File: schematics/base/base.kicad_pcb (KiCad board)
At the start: 2 copper layers, 96.5 x 96.5 mm, 72 parts, among them J1 Bionic_ZIF_Socket_48pin, P10 P10, P11 P11, P12 P12, P13 P13, P14 P14, P15 P15, P16 P16, P17 P17, P20 P20, P21 P21, P22 P23, P23 P24, P24 P25, P25 P26, P26 P27, P27 P28, P30 P30, P31 P31, P32 P32, P33 P33, P34 P34, P35 P35, P36 P36, P37 P37, P40 P40, P41 P41, P42 P42, P43 P43, P44 P44, P45 P45, P46 P46, P47 P47, P50 P50, P51 P51, P52 P52, P53 P53, P54 P54, P55 P55, P56 P56, P57 P57, SW2 USR_SW, U1 TXS0108EPW, U2 TXS0108EPW, U3 TXS0108EPW, U4 TXS0108EPW, U5 TXS0108EPW, U6 SN74ACT1071DR, U7 SN74ACT1071DR

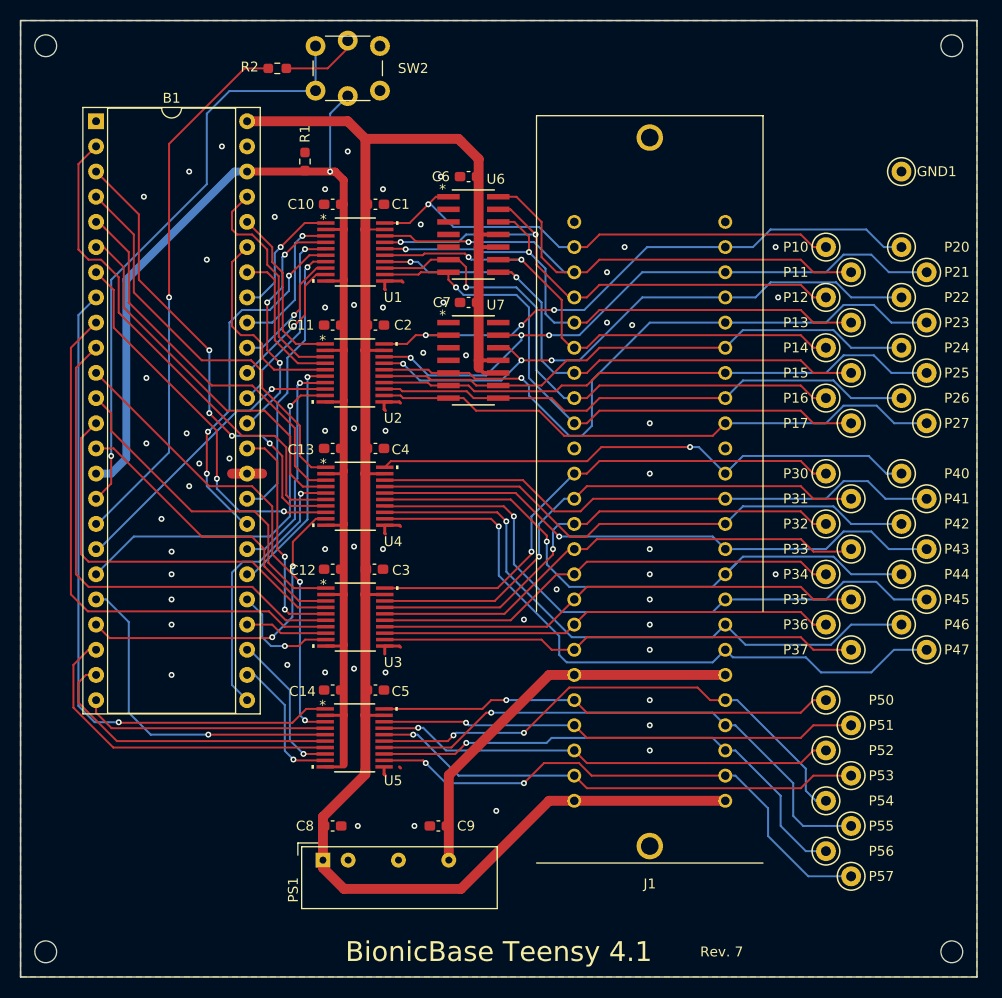
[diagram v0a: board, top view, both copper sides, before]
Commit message: [Base] Add USB-C Power connector
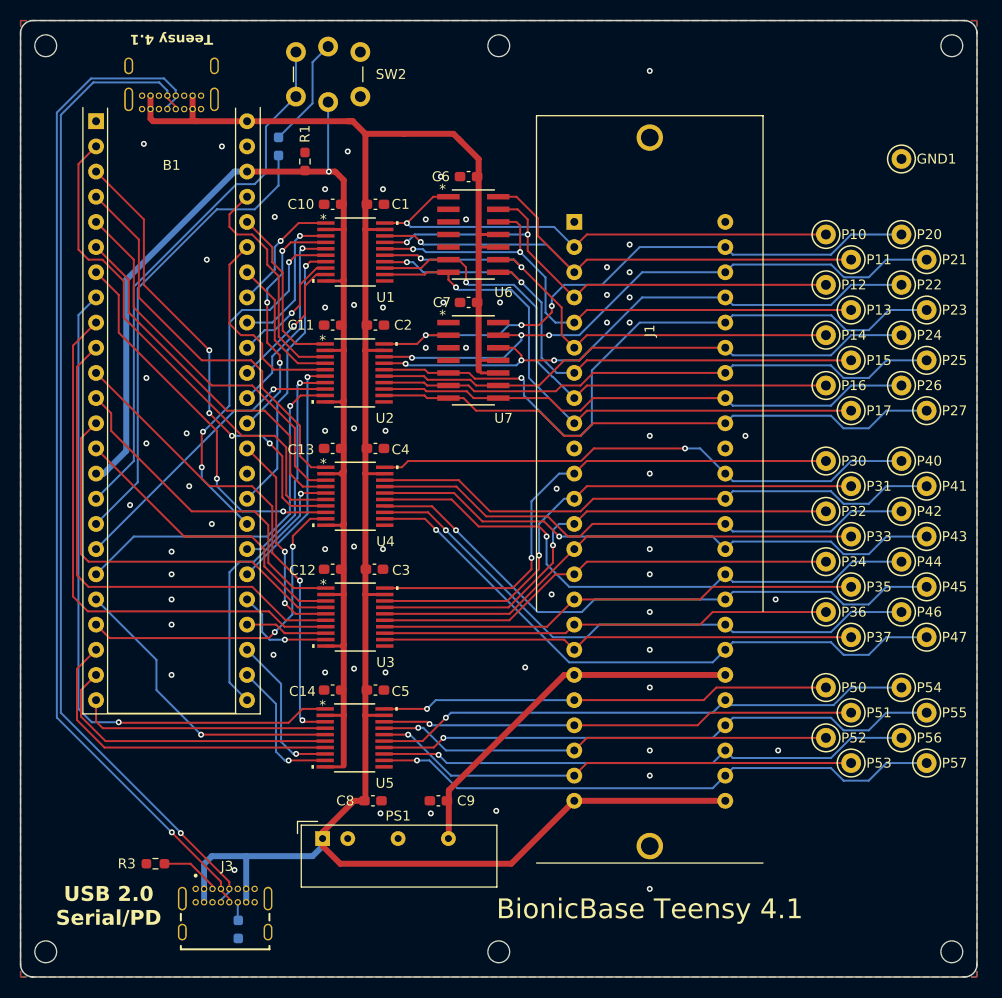
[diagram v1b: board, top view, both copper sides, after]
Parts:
- added J2: USB_C_USB2.0_16P, 0-LocalLibrary:GCT_USB4085-GF-A_REVB, B.Cu at (88.3, 46.6)
- added J3: USB_C_USB2.0_16P, 0-LocalLibrary:GCT_USB4085-GF-A_REVB, F.Cu at (93.7, 134.1)
- added MH2: MountingHole_2.2mm_M2, MountingHole:MountingHole_2.2mm_M2, F.Cu at (121.3, 136.0)
- added MH2: MountingHole_2.2mm_M2, MountingHole:MountingHole_2.2mm_M2, F.Cu at (121.3, 44.6)
- added R3: 5.1k, Resistor_SMD:R_0603_1608Metric_Pad0.98x0.95mm_HandSolder, F.Cu at (86.7, 127.2)
- added R4: 5.1k, Resistor_SMD:R_0603_1608Metric_Pad0.98x0.95mm_HandSolder, B.Cu at (95.0, 133.8)
- B1: footprint 0-LocalLibrary:DIP-48_W15.24mm_Socket -> 0-LocalLibrary:Teensy 4.1
- GND1: value GND -> TP; footprint TestPoint:TestPoint_Keystone_5000-5004_Miniature -> 0-LocalLibrary:TestPoint_Keystone_5001-black
- P10: value P10 -> TP; footprint TestPoint:TestPoint_Keystone_5000-5004_Miniature -> 0-LocalLibrary:TestPoint_Keystone_5001-black
- P11: value P11 -> TP; footprint TestPoint:TestPoint_Keystone_5000-5004_Miniature -> 0-LocalLibrary:TestPoint_Keystone_5115-brown
- P12: value P12 -> TP; footprint TestPoint:TestPoint_Keystone_5000-5004_Miniature -> 0-LocalLibrary:TestPoint_Keystone_5000-red
- P13: value P13 -> TP; footprint TestPoint:TestPoint_Keystone_5000-5004_Miniature -> 0-LocalLibrary:TestPoint_Keystone_5004-yellow
- P14: value P14 -> TP; footprint TestPoint:TestPoint_Keystone_5000-5004_Miniature -> 0-LocalLibrary:TestPoint_Keystone_5003-orange
- P15: value P15 -> TP; footprint TestPoint:TestPoint_Keystone_5000-5004_Miniature -> 0-LocalLibrary:TestPoint_Keystone_5116-green
- P16: value P16 -> TP; footprint TestPoint:TestPoint_Keystone_5000-5004_Miniature -> 0-LocalLibrary:TestPoint_Keystone_5117-blue
- P17: value P17 -> TP; footprint TestPoint:TestPoint_Keystone_5000-5004_Miniature -> 0-LocalLibrary:TestPoint_Keystone_5119-purple
- P20: value P20 -> TP; footprint TestPoint:TestPoint_Keystone_5000-5004_Miniature -> 0-LocalLibrary:TestPoint_Keystone_5001-black
- P21: value P21 -> TP; footprint TestPoint:TestPoint_Keystone_5000-5004_Miniature -> 0-LocalLibrary:TestPoint_Keystone_5115-brown
- P22: value P23 -> TP; footprint TestPoint:TestPoint_Keystone_5000-5004_Miniature -> 0-LocalLibrary:TestPoint_Keystone_5000-red
- P23: value P24 -> TP; footprint TestPoint:TestPoint_Keystone_5000-5004_Miniature -> 0-LocalLibrary:TestPoint_Keystone_5004-yellow
- P24: value P25 -> TP; footprint TestPoint:TestPoint_Keystone_5000-5004_Miniature -> 0-LocalLibrary:TestPoint_Keystone_5003-orange
- P25: value P26 -> TP; footprint TestPoint:TestPoint_Keystone_5000-5004_Miniature -> 0-LocalLibrary:TestPoint_Keystone_5116-green
- P26: value P27 -> TP; footprint TestPoint:TestPoint_Keystone_5000-5004_Miniature -> 0-LocalLibrary:TestPoint_Keystone_5117-blue
- P27: value P28 -> TP; footprint TestPoint:TestPoint_Keystone_5000-5004_Miniature -> 0-LocalLibrary:TestPoint_Keystone_5119-purple
- P30: value P30 -> TP; footprint TestPoint:TestPoint_Keystone_5000-5004_Miniature -> 0-LocalLibrary:TestPoint_Keystone_5001-black
- P31: value P31 -> TP; footprint TestPoint:TestPoint_Keystone_5000-5004_Miniature -> 0-LocalLibrary:TestPoint_Keystone_5115-brown
- P32: value P32 -> TP; footprint TestPoint:TestPoint_Keystone_5000-5004_Miniature -> 0-LocalLibrary:TestPoint_Keystone_5000-red
- P33: value P33 -> TP; footprint TestPoint:TestPoint_Keystone_5000-5004_Miniature -> 0-LocalLibrary:TestPoint_Keystone_5004-yellow
- P34: value P34 -> TP; footprint TestPoint:TestPoint_Keystone_5000-5004_Miniature -> 0-LocalLibrary:TestPoint_Keystone_5003-orange
- P35: value P35 -> TP; footprint TestPoint:TestPoint_Keystone_5000-5004_Miniature -> 0-LocalLibrary:TestPoint_Keystone_5116-green
- P36: value P36 -> TP; footprint TestPoint:TestPoint_Keystone_5000-5004_Miniature -> 0-LocalLibrary:TestPoint_Keystone_5117-blue
- P37: value P37 -> TP; footprint TestPoint:TestPoint_Keystone_5000-5004_Miniature -> 0-LocalLibrary:TestPoint_Keystone_5119-purple
- P40: value P40 -> TP; footprint TestPoint:TestPoint_Keystone_5000-5004_Miniature -> 0-LocalLibrary:TestPoint_Keystone_5001-black
- P41: value P41 -> TP; footprint TestPoint:TestPoint_Keystone_5000-5004_Miniature -> 0-LocalLibrary:TestPoint_Keystone_5115-brown
- P42: value P42 -> TP; footprint TestPoint:TestPoint_Keystone_5000-5004_Miniature -> 0-LocalLibrary:TestPoint_Keystone_5000-red
- P43: value P43 -> TP; footprint TestPoint:TestPoint_Keystone_5000-5004_Miniature -> 0-LocalLibrary:TestPoint_Keystone_5004-yellow
- P44: value P44 -> TP; footprint TestPoint:TestPoint_Keystone_5000-5004_Miniature -> 0-LocalLibrary:TestPoint_Keystone_5003-orange
- P45: value P45 -> TP; footprint TestPoint:TestPoint_Keystone_5000-5004_Miniature -> 0-LocalLibrary:TestPoint_Keystone_5116-green
- P46: value P46 -> TP; footprint TestPoint:TestPoint_Keystone_5000-5004_Miniature -> 0-LocalLibrary:TestPoint_Keystone_5117-blue
- P47: value P47 -> TP; footprint TestPoint:TestPoint_Keystone_5000-5004_Miniature -> 0-LocalLibrary:TestPoint_Keystone_5119-purple
- P50: value P50 -> TP; footprint TestPoint:TestPoint_Keystone_5000-5004_Miniature -> 0-LocalLibrary:TestPoint_Keystone_5001-black
- P51: value P51 -> TP; footprint TestPoint:TestPoint_Keystone_5000-5004_Miniature -> 0-LocalLibrary:TestPoint_Keystone_5115-brown
- P52: value P52 -> TP; footprint TestPoint:TestPoint_Keystone_5000-5004_Miniature -> 0-LocalLibrary:TestPoint_Keystone_5000-red
- P53: value P53 -> TP; footprint TestPoint:TestPoint_Keystone_5000-5004_Miniature -> 0-LocalLibrary:TestPoint_Keystone_5004-yellow
- P54: value P54 -> TP; footprint TestPoint:TestPoint_Keystone_5000-5004_Miniature -> 0-LocalLibrary:TestPoint_Keystone_5003-orange
- P55: value P55 -> TP; footprint TestPoint:TestPoint_Keystone_5000-5004_Miniature -> 0-LocalLibrary:TestPoint_Keystone_5116-green
- P56: value P56 -> TP; footprint TestPoint:TestPoint_Keystone_5000-5004_Miniature -> 0-LocalLibrary:TestPoint_Keystone_5117-blue
- P57: value P57 -> TP; footprint TestPoint:TestPoint_Keystone_5000-5004_Miniature -> 0-LocalLibrary:TestPoint_Keystone_5119-purple
- R2: moved to B.Cu
- moved P55 13.7 mm to (164.5, 111.9)
- moved P54 13.7 mm to (162.0, 109.4)
- moved P56 13.7 mm to (162.0, 114.5)
- moved P57 13.7 mm to (164.5, 117.0)
- moved R2 7.88 mm to (99.1, 54.8), turned to -90 degrees
- moved C8 4.79 mm to (108.6, 120.8)
- moved C9 2.54 mm to (115.2, 120.8)
- moved PS1 2.18 mm to (103.5, 124.6)
- moved SW2 2.07 mm to (107.3, 49.7)
- moved P13 1.27 mm to (156.9, 71.3)
- moved P15 1.27 mm to (156.9, 76.3)
- moved P23 1.27 mm to (164.5, 71.3)
- moved P25 1.27 mm to (164.5, 76.3)
- moved P33 1.27 mm to (156.9, 94.1)
- moved P35 1.27 mm to (156.9, 99.2)
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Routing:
- net Net-(J2-D+-PadA6): track 0.00 -> 103.1 mm, vias 0 -> 1
- net Net-(J2-D--PadA7): track 0.00 -> 101.5 mm, vias 0 -> 1
- net VCC: track 187.3 -> 222.2 mm
- net GND: track 14.7 -> 0.00 mm, vias 60 -> 66
- net Net-(B1-P6.13): track 54.7 -> 47.1 mm, vias 1 -> 0
- net Net-(J3-CC1): track 0.00 -> 6.08 mm
- net Net-(B1-P6.12): track 59.9 -> 54.5 mm, vias 1 -> 0
- net /+15V: track 42.3 -> 37.6 mm
- net /P47: track 67.1 -> 62.8 mm
- net Net-(B1-P8.18): track 34.1 -> 30.6 mm
- net /P46: track 62.6 -> 59.0 mm
- net Net-(SW2-K): track 7.82 -> 11.2 mm
- net /P45: track 63.9 -> 61.2 mm
- net /P57: track 55.3 -> 58.0 mm, vias 2 -> 1
- net /P56: track 51.8 -> 54.3 mm
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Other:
- outline, holes or cut-outs redrawn
- board text added: "JLCJLCJLCJLC"
- board text added: "Rev. 8"
- board text added: "Teensy 4.1"
- board text added: "USB 2.0 Serial/PD"
- board text removed: "Rev. 7"

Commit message: [Base] Change mount hale to M3
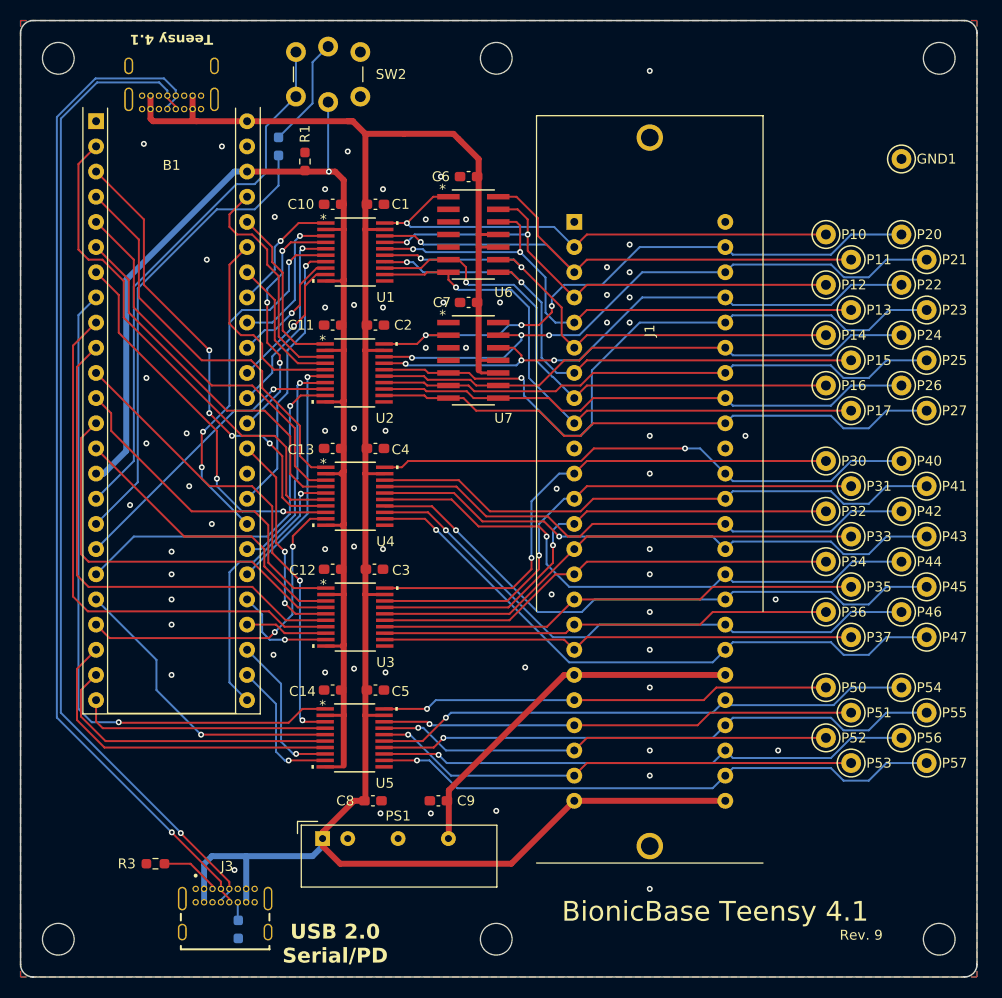
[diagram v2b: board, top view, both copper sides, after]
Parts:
- removed the MH1 at (75.6, 44.6)
- removed MH2 (x3), MH3, MH4: MountingHole_2.2mm_M2, MountingHole:MountingHole_2.2mm_M2
- added MH1: MountingHole_3.2mm_M3, MountingHole:MountingHole_3.2mm_M3, F.Cu at (165.8, 45.9)
- added MH1: MountingHole_3.2mm_M3, MountingHole:MountingHole_3.2mm_M3, F.Cu at (165.8, 134.8)
- added MH1: MountingHole_3.2mm_M3, MountingHole:MountingHole_3.2mm_M3, F.Cu at (121.1, 134.8)
- added MH1: MountingHole_3.2mm_M3, MountingHole:MountingHole_3.2mm_M3, F.Cu at (76.9, 134.8)
- added MH1: MountingHole_3.2mm_M3, MountingHole:MountingHole_3.2mm_M3, F.Cu at (76.9, 45.9)
- added MH1: MountingHole_3.2mm_M3, MountingHole:MountingHole_3.2mm_M3, F.Cu at (121.1, 45.9)
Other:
- board text added: "Rev. 9"
- board text removed: "Rev. 8"

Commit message: [base] Fix push switch foot print
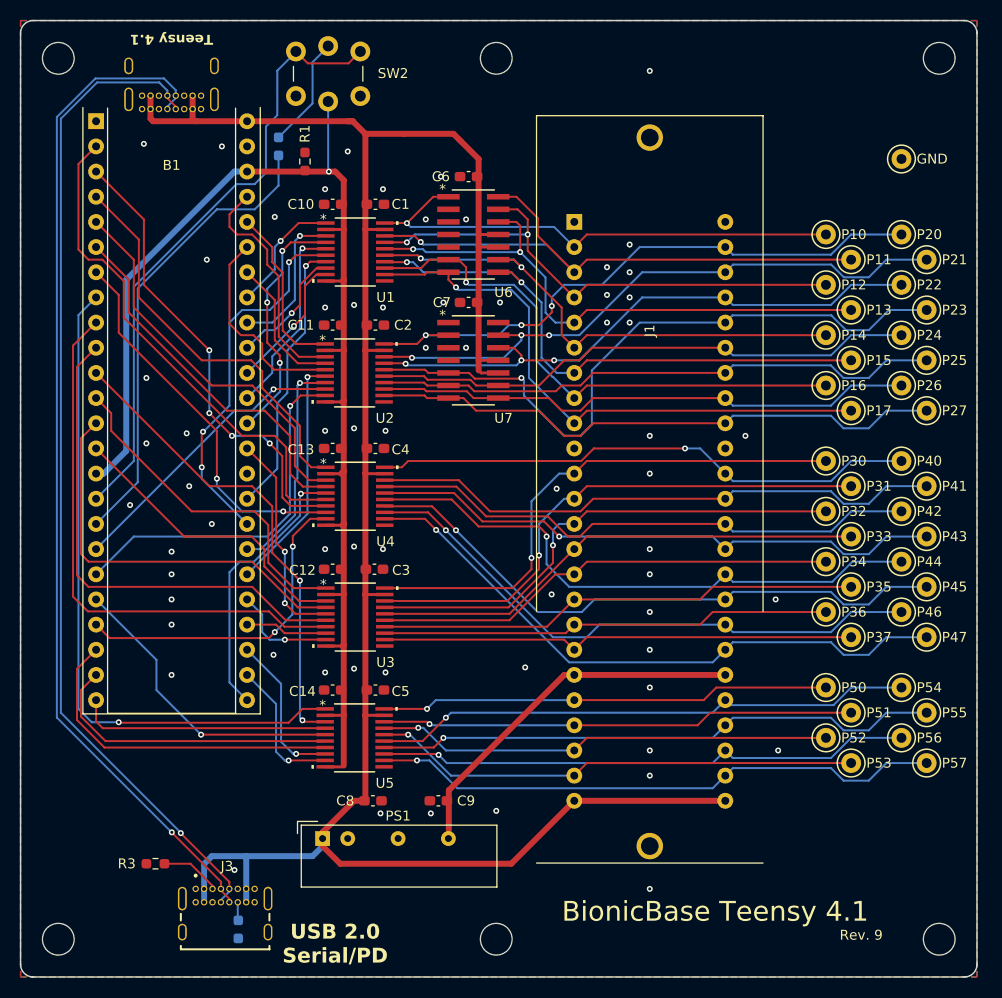
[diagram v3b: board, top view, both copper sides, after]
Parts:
- moved SW2 7.94 mm to (100.8, 45.2), turned to 0 degrees
- renumbered GND1 to GND
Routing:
- net Net-(B1-P6.12): track 54.5 -> 62.0 mm

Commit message: [base] Change test points to pin headers
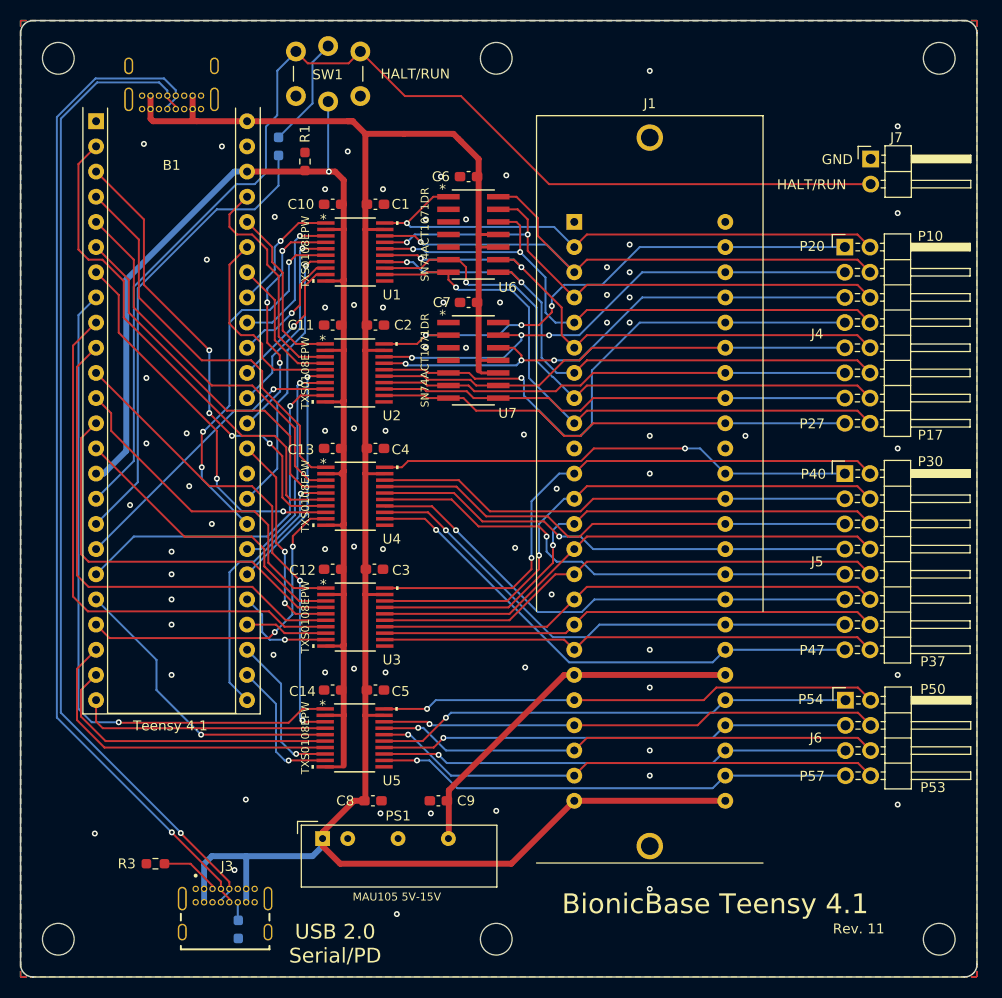
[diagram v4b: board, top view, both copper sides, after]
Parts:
- removed GND, P10, P20, P30, P40, P50: TP, 0-LocalLibrary:TestPoint_Keystone_5001-black
- removed P11, P21, P31, P41, P51: TP, 0-LocalLibrary:TestPoint_Keystone_5115-brown
- removed P12, P22, P32, P42, P52: TP, 0-LocalLibrary:TestPoint_Keystone_5000-red
- removed P13, P23, P33, P43, P53: TP, 0-LocalLibrary:TestPoint_Keystone_5004-yellow
- removed P14, P24, P34, P44, P54: TP, 0-LocalLibrary:TestPoint_Keystone_5003-orange
- removed P15, P25, P35, P45, P55: TP, 0-LocalLibrary:TestPoint_Keystone_5116-green
- removed P16, P26, P36, P46, P56: TP, 0-LocalLibrary:TestPoint_Keystone_5117-blue
- removed P17, P27, P37, P47, P57: TP, 0-LocalLibrary:TestPoint_Keystone_5119-purple
- removed SW2: USR_SW, 0-LocalLibrary:SW_PUSH_LED_6mm
- added J4: P1/P2, Connector_PinHeader_2.54mm:PinHeader_2x08_P2.54mm_Horizontal, F.Cu at (156.2, 64.9)
- added J5: P3/P4, Connector_PinHeader_2.54mm:PinHeader_2x08_P2.54mm_Horizontal, F.Cu at (156.2, 87.8)
- added J6: P5, Connector_PinHeader_2.54mm:PinHeader_2x04_P2.54mm_Horizontal, F.Cu at (156.3, 110.7)
- added J7: P6, Connector_PinHeader_2.54mm:PinHeader_1x02_P2.54mm_Horizontal, F.Cu at (158.9, 56.0)
- added SW1: USR_SW, 0-LocalLibrary:SW_PUSH_LED_6mm, F.Cu at (100.8, 45.2)
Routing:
- net Net-(B1-P6.12): track 62.0 -> 119.1 mm
- net /P23: track 68.9 -> 58.9 mm
- net /P21: track 63.3 -> 53.5 mm
- net /P45: track 61.2 -> 51.4 mm
- net /P43: track 58.6 -> 48.8 mm
- net /P47: track 62.8 -> 53.0 mm
- net /P41: track 58.1 -> 48.3 mm
- net /P27: track 58.5 -> 48.7 mm
- net /P25: track 57.5 -> 47.6 mm
- net /P57: track 58.0 -> 48.3 mm
- net /P55: track 57.3 -> 47.5 mm
- net /P44: track 59.3 -> 50.6 mm
- net /P46: track 59.0 -> 52.2 mm
- net /P42: track 55.9 -> 49.0 mm
- net /P24: track 55.3 -> 48.5 mm
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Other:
- board text added: "GND"
- board text added: "HALT/RUN"
- board text added: "MAU105 5V-15V"
- board text added: "P10"
- board text added: "P17"
- board text added: "P20"
- board text added: "P27"
- board text added: "P30"
- board text added: "P37"
- board text added: "P40"
- board text added: "P47"
- board text added: "P50"
- board text added: "P53"
- board text added: "P54"
- board text added: "P57"
- board text added: "Rev. 11"
- board text added: "SN74ACT1071DR"
- board text added: "TXS0108EPW"
- board text removed: "Rev. 9"
